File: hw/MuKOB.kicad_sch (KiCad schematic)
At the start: 46 parts, among them J10 Conn_01x04, J11 Conn_01x07, J3 Micro_SD_Card, J6 Conn_01x03, J7 SER_COM, J8 SJ-43516-SMT-TR, J9 Conn_01x02, Q2 2N3904, SW1 RESET, U1 TLV70033_SOT23-5, U2 PicoW, U3 NC7WZ16P6X, U5 MAX3221

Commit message: Schematic updates.
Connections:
- net GND: no longer C15.1, J8.T, R8.2
- net I2C0_SCL: now also J10.3 (Pin_3); no longer J10.4 (Pin_4)
- net I2C0_SDA: now also J10.4 (Pin_4); no longer J10.3 (Pin_3)
- net PWM_LL: now also C15.2, C8.1, R2.1, R4.2; no longer C14.2, C7.1, R1.1, R3.2
- net PWM_RR: now also C14.2, C7.1, R1.1, R3.2; no longer C15.2, C8.1, R2.1, R4.2
- net at J8.R1N: no longer LS1.1
- net at J8.TN: now also LS1.1
- new net PWM_AUDIO_L: C15.1, J8.T, R8.2
- no-connect marks 5 -> 6
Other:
- note added: "3.5mm TRRS Audio (STD)"
- note added: "Audio Output Option"
- note added: "Audio Section"
- note added: "Mic input (optional)"
- note added: "Needed for Analog out and/or Mic in"
- note added: "Place JR1+BZ1 or JR2+rest"
- note removed: "Audio Power"
- note removed: "Place JR1+BZ1 or JR2+LS1"
- note removed: "STD TRRS 3.5mm Audio"
- moved on the sheet: BZ1, C1, C10, C11, C12, C13, C14, C15, C16, C17, C2, C7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

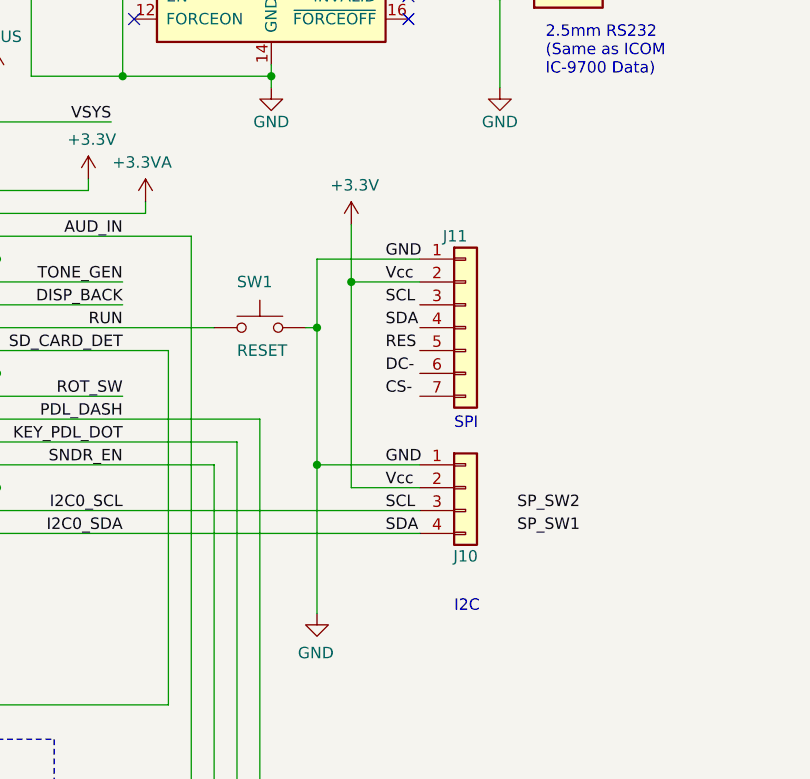
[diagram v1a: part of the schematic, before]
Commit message: Update and organize display component docs.
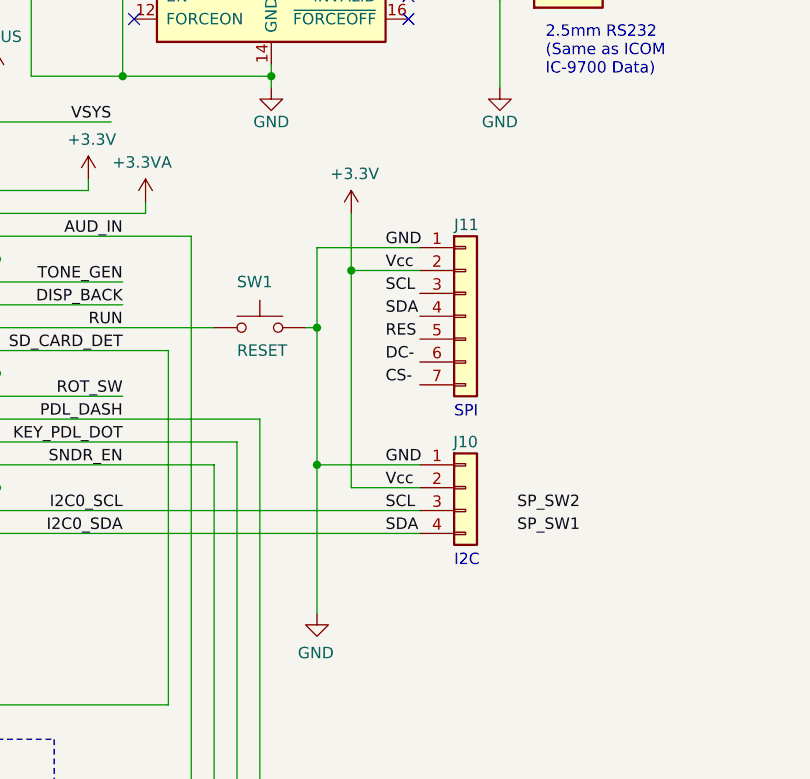
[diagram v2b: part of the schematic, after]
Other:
- moved on the sheet: J11
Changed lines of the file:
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@@
   (junction (at 31.75 173.99) (diameter 0) (color 0 0 0 0)
   )
-  (junction (at 191.77 87.63) (diameter 0) (color 0 0 0 0)
+  (junction (at 191.77 86.36) (diameter 0) (color 0 0 0 0)
   )
   (junction (at 208.28 45.72) (diameter 0) (color 0 0 0 0)
@@
     (stroke (width 0) (type default))
   )
-  (wire (pts (xy 187.96 92.71) (xy 187.96 85.09))
+  (wire (pts (xy 187.96 92.71) (xy 187.96 83.82))
     (stroke (width 0) (type default))
   )
@@
     (stroke (width 0) (type default))
   )
-  (wire (pts (xy 191.77 87.63) (xy 191.77 81.28))
+  (wire (pts (xy 191.77 86.36) (xy 191.77 80.01))
     (stroke (width 0) (type default))
   )
@@
     (stroke (width 0) (type default))
   )
-  (wire (pts (xy 191.77 87.63) (xy 199.39 87.63))
+  (wire (pts (xy 191.77 86.36) (xy 199.39 86.36))
     (stroke (width 0) (type default))
   )
@@
     (stroke (width 0) (type default))
   )
-  (wire (pts (xy 187.96 85.09) (xy 199.39 85.09))
+  (wire (pts (xy 187.96 83.82) (xy 199.39 83.82))
     (stroke (width 0) (type default))
   )
@@
     (stroke (width 0) (type default))
   )
-  (wire (pts (xy 191.77 87.63) (xy 191.77 110.49))
+  (wire (pts (xy 191.77 86.36) (xy 191.77 110.49))
     (stroke (width 0) (type default))
   )
@@
     (effects (font (size 1.27 1.27)) (justify left bottom))
   )
-  (text "I2C" (at 203.2 124.46 0)
+  (text "I2C" (at 203.2 119.38 0)
     (effects (font (size 1.27 1.27)) (justify left bottom))
   )
@@
     (effects (font (size 1.27 1.27) (color 194 0 194 1)) (justify left bottom))
   )
-  (text "SPI" (at 203.2 104.14 0)
+  (text "SPI" (at 203.2 102.87 0)
     (effects (font (size 1.27 1.27)) (justify left bottom))
   )
@@
     (effects (font (size 1.27 1.27)) (justify left bottom))
   )
-  (label "SCL" (at 195.58 90.17 0) (fields_autoplaced)
+  (label "SCL" (at 195.58 88.9 0) (fields_autoplaced)
     (effects (font (size 1.27 1.27)) (justify left bottom))
   )
@@
     (effects (font (size 1.27 1.27)) (justify right bottom))
   )
-  (label "CS-" (at 195.58 100.33 0) (fields_autoplaced)
+  (label "CS-" (at 195.58 99.06 0) (fields_autoplaced)
     (effects (font (size 1.27 1.27)) (justify left bottom))
   )
@@
     (effects (font (size 1.27 1.27)) (justify left bottom))
   )
-  (label "RES" (at 195.58 95.25 0) (fields_autoplaced)
+  (label "RES" (at 195.58 93.98 0) (fields_autoplaced)
     (effects (font (size 1.27 1.27)) (justify left bottom))
   )
@@
     (effects (font (size 1.27 1.27)) (justify right bottom))
   )
-  (label "SDA" (at 195.58 92.71 0) (fields_autoplaced)
+  (label "SDA" (at 195.58 91.44 0) (fields_autoplaced)
     (effects (font (size 1.27 1.27)) (justify left bottom))
   )
@@
     (effects (font (size 1.27 1.27)) (justify left bottom))
   )
-  (label "DC-" (at 195.58 97.79 0) (fields_autoplaced)
+  (label "DC-" (at 195.58 96.52 0) (fields_autoplaced)
     (effects (font (size 1.27 1.27)) (justify left bottom))
   )
@@
     (effects (font (size 1.27 1.27)) (justify left bottom))
   )
-  (label "Vcc" (at 195.58 87.63 0) (fields_autoplaced)
+  (label "Vcc" (at 195.58 86.36 0) (fields_autoplaced)
     (effects (font (size 1.27 1.27)) (justify left bottom))
   )
@@
     (effects (font (size 1.27 1.27)) (justify left bottom))
   )
-  (label "GND" (at 195.58 85.09 0) (fields_autoplaced)
+  (label "GND" (at 195.58 83.82 0) (fields_autoplaced)
     (effects (font (size 1.27 1.27)) (justify left bottom))
   )
@@
     )
   )
-  (symbol (lib_id "Connector_Generic:Conn_01x07") (at 204.47 92.71 0) (unit 1)
-    (in_bom yes) (on_board yes) (dnp no)
-    (property "Reference" "J11" (at 201.93 82.55 0)
-      (effects (font (size 1.27 1.27)) (justify left))
-    )
-    (property "Value" "Conn_01x07" (at 207.01 94.615 0)
+  (symbol (lib_id "Connector_Generic:Conn_01x07") (at 204.47 91.44 0) (unit 1)
+    (in_bom yes) (on_board yes) (dnp no)
+    (property "Reference" "J11" (at 203.2 81.28 0)
+      (effects (font (size 1.27 1.27)) (justify left))
+    )
+    (property "Value" "Conn_01x07" (at 207.01 93.345 0)
       (effects (font (size 1.27 1.27)) (justify left) hide)
     )
-    (property "Footprint" "" (at 204.47 92.71 0)
-      (effects (font (size 1.27 1.27)) hide)
-    )
-    (property "Datasheet" "~" (at 204.47 92.71 0)
+    (property "Footprint" "" (at 204.47 91.44 0)
+      (effects (font (size 1.27 1.27)) hide)
+    )
+    (property "Datasheet" "~" (at 204.47 91.44 0)
       (effects (font (size 1.27 1.27)) hide)
     )
@@
   (symbol (lib_id "Connector_Generic:Conn_01x04") (at 204.47 110.49 0) (unit 1)
     (in_bom yes) (on_board yes) (dnp no)
-    (property "Reference" "J10" (at 204.47 118.11 0)
+    (property "Reference" "J10" (at 204.47 105.41 0)
       (effects (font (size 1.27 1.27)))
     )
@@
     )
   )
-  (symbol (lib_id "power:+3.3V") (at 191.77 81.28 0) (unit 1)
-    (in_bom yes) (on_board yes) (dnp no)
-    (property "Reference" "#PWR024" (at 191.77 85.09 0)
-      (effects (font (size 1.27 1.27)) hide)
-    )
-    (property "Value" "+3.3V" (at 192.151 76.8858 0)
-      (effects (font (size 1.27 1.27)))
-    )
-    (property "Footprint" "" (at 191.77 81.28 0)
-      (effects (font (size 1.27 1.27)) hide)
-    )
-    (property "Datasheet" "" (at 191.77 81.28 0)
-      (effects (font (size 1.27 1.27)) hide)
-    )
+  (symbol (lib_id "power:+3.3V") (at 191.77 80.01 0) (unit 1)
+    (in_bom yes) (on_board yes) (dnp no)
+    (property "Reference" "#PWR024" (at 191.77 83.82 0)
+      (effects (font (size 1.27 1.27)) hide)
+    )
+    (property "Value" "+3.3V" (at 192.151 75.6158 0)
+      (effects (font (size 1.27 1.27)))
+    )
+    (property "Footprint" "" (at 191.77 80.01 0)
+      (effects (font (size 1.27 1.27)) hide)
+    )
+    (property "Datasheet" "" (at 191.77 80.01 0)
+      (effects (font (size 1.27 1.27)) hide)
+    )

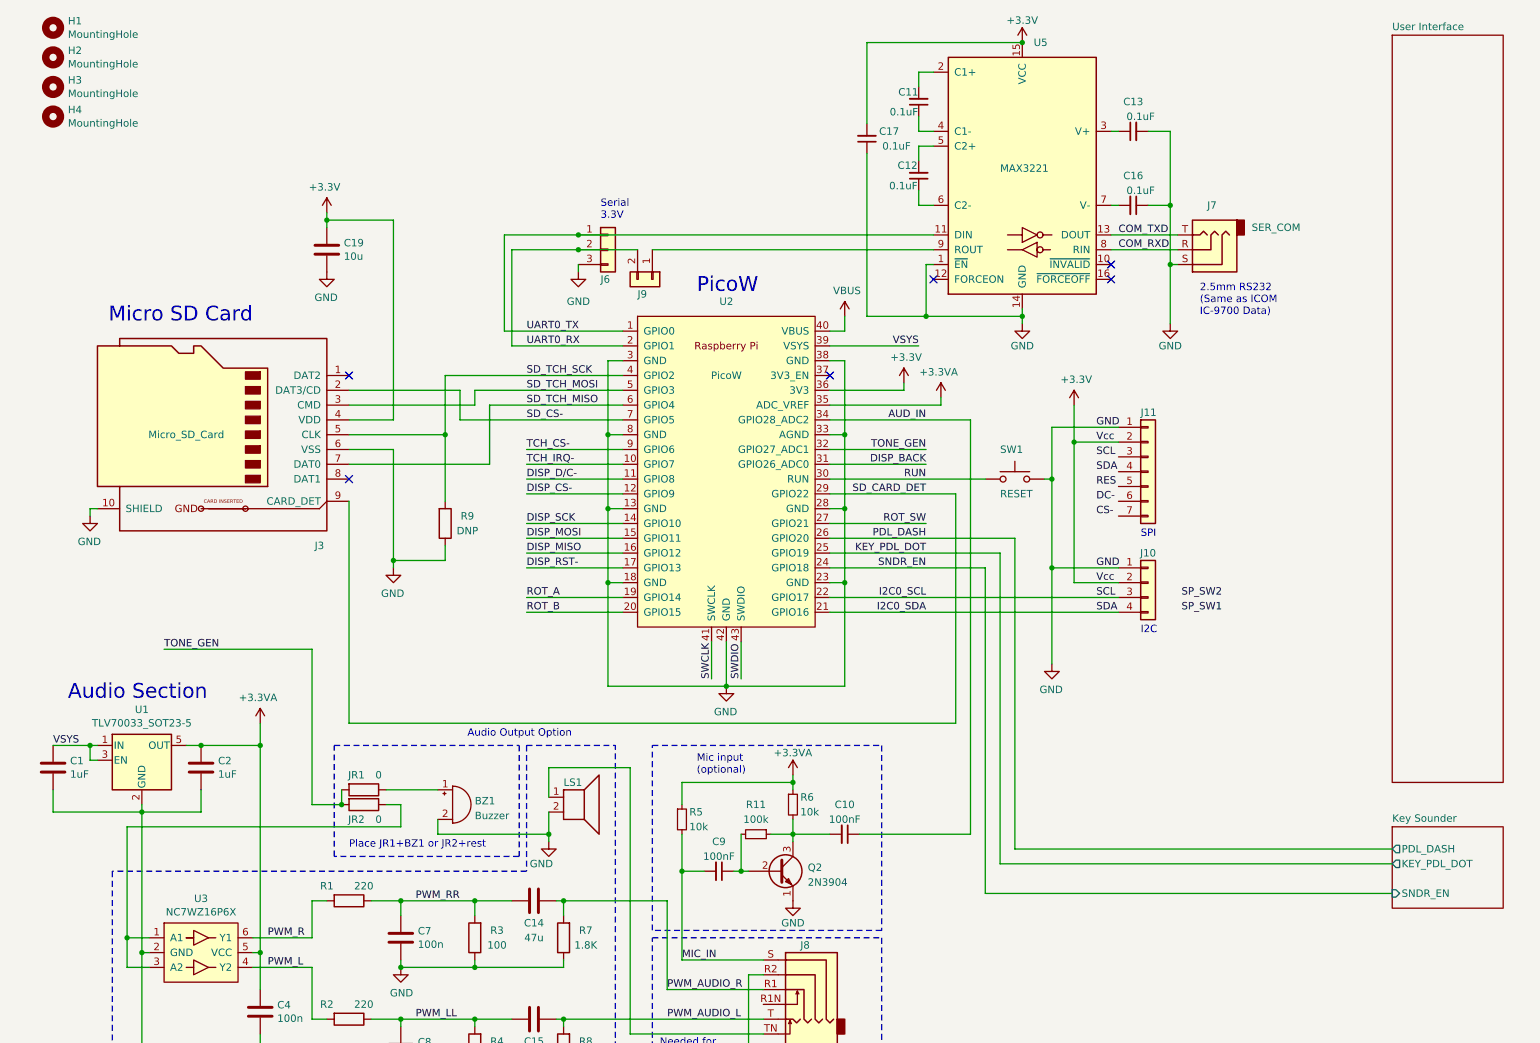
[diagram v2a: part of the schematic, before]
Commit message: HW - Display FFCs.
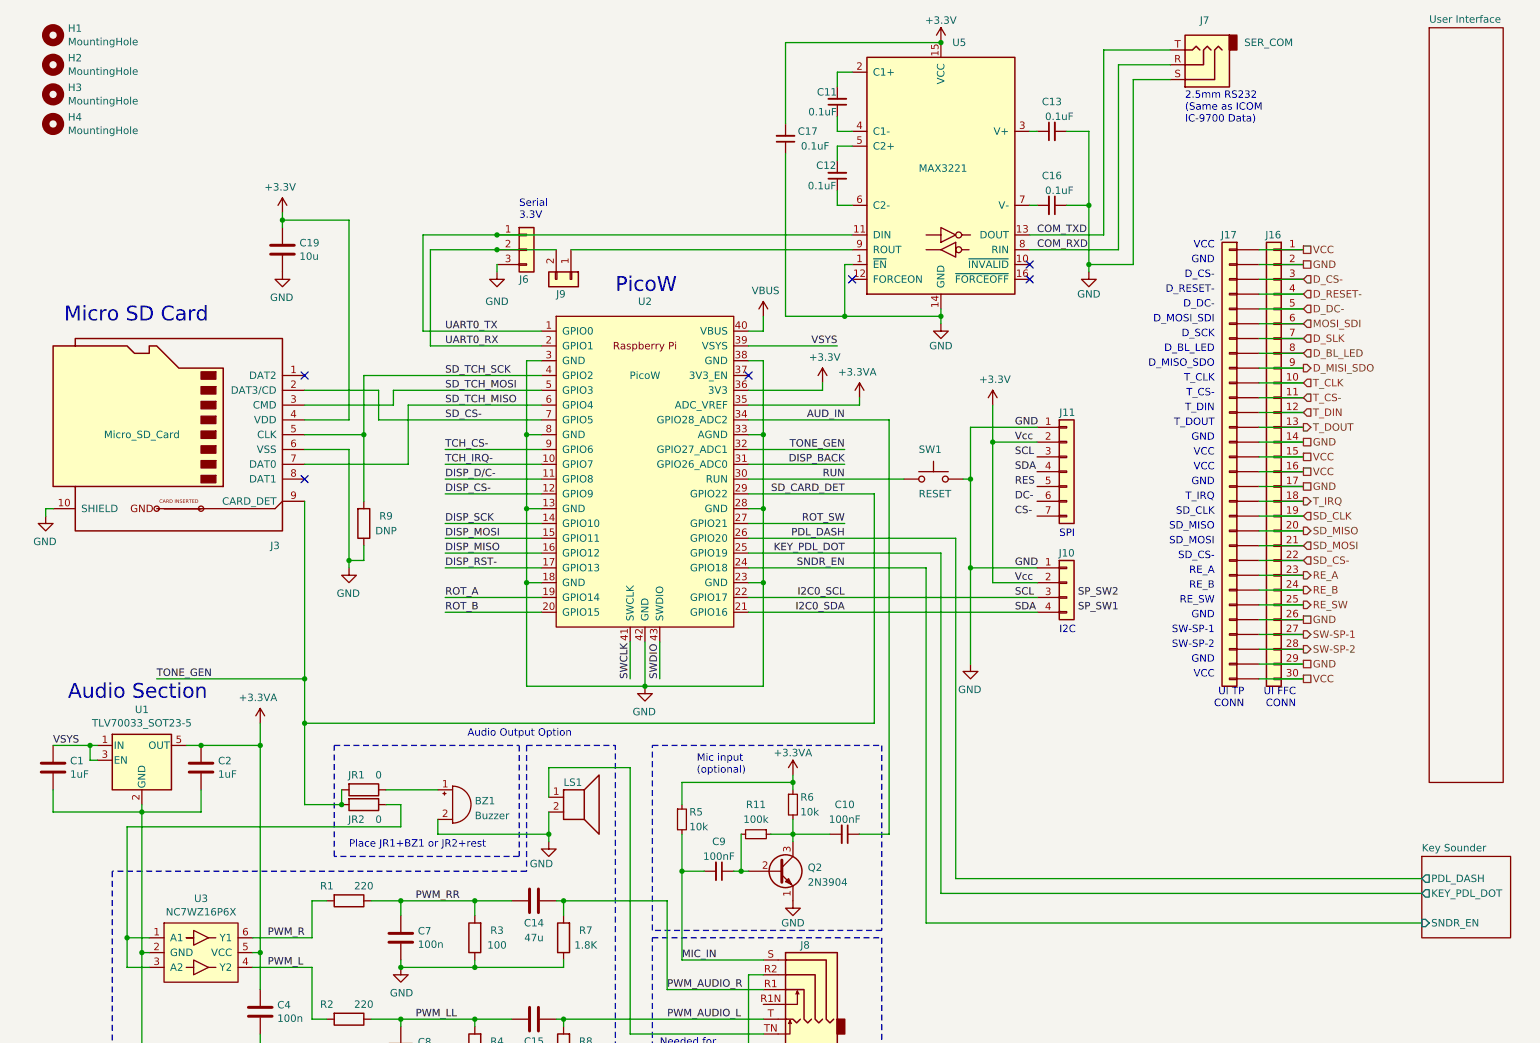
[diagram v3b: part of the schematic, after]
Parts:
- added J16, J17: Conn_01x30, symbol Connector_Generic:Conn_01x30
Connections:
- net TONE_GEN is gone; now on net SD_CARD_DET: JR1.2, JR2.2, U2.32 (GPIO27_ADC1)
- net GND: now also J16.14 (Pin_14), J16.17 (Pin_17), J16.2 (Pin_2), J16.26 (Pin_26), J16.29 (Pin_29), J17.14 (Pin_14), J17.17 (Pin_17), J17.2 (Pin_2), J17.26 (Pin_26), J17.29 (Pin_29)
- net SD_CS-: now also J16.22 (Pin_22), J17.22 (Pin_22)
- new net D_BL_LED: J16.8 (Pin_8), J17.8 (Pin_8)
- new net D_CS-: J16.3 (Pin_3), J17.3 (Pin_3)
- new net D_DC-: J16.5 (Pin_5), J17.5 (Pin_5)
- new net D_MISI_SDO: J16.9 (Pin_9), J17.9 (Pin_9)
- new net D_RESET-: J16.4 (Pin_4), J17.4 (Pin_4)
- new net D_SLK: J16.7 (Pin_7), J17.7 (Pin_7)
- new net MOSI_SDI: J16.6 (Pin_6), J17.6 (Pin_6)
- new net RE_A: J16.23 (Pin_23), J17.23 (Pin_23)
- new net RE_B: J16.24 (Pin_24), J17.24 (Pin_24)
- new net RE_SW: J16.25 (Pin_25), J17.25 (Pin_25)
- new net SD_CLK: J16.19 (Pin_19), J17.19 (Pin_19)
- new net SD_MISO: J16.20 (Pin_20), J17.20 (Pin_20)
- new net SD_MOSI: J16.21 (Pin_21), J17.21 (Pin_21)
- new net SW-SP-1: J16.27 (Pin_27), J17.27 (Pin_27)
- new net SW-SP-2: J16.28 (Pin_28), J17.28 (Pin_28)
- new net T_CLK: J16.10 (Pin_10), J17.10 (Pin_10)
- new net T_CS-: J16.11 (Pin_11), J17.11 (Pin_11)
- new net T_DIN: J16.12 (Pin_12), J17.12 (Pin_12)
- new net T_DOUT: J16.13 (Pin_13), J17.13 (Pin_13)
- new net T_IRQ: J16.18 (Pin_18), J17.18 (Pin_18)
- new net VCC: J16.1 (Pin_1), J16.15 (Pin_15), J16.16 (Pin_16), J16.30 (Pin_30), J17.1 (Pin_1), J17.15 (Pin_15), J17.16 (Pin_16), J17.30 (Pin_30)
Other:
- note added: "D_BL_LED"
- note added: "D_CS-"
- note added: "D_DC-"
- note added: "D_MISO_SDO"
- note added: "D_MOSI_SDI"
- note added: "D_RESET-"
- note added: "D_SCK"
- note added: "GND"
- note added: "RE_A"
- note added: "RE_B"
- note added: "RE_SW"
- note added: "SD_CLK"
- note added: "SD_CS-"
- note added: "SD_MISO"
- note added: "SD_MOSI"
- note added: "SW-SP-1"
- note added: "SW-SP-2"
- note added: "T_CLK"
- note added: "T_CS-"
- note added: "T_DIN"
- note added: "T_DOUT"
- note added: "T_IRQ"
- note added: "UI FFC CONN"
- note added: "UI TP CONN"
- note added: "VCC"
- moved on the sheet: C11, C12, C13, C16, C17, C19, H1, H2, H3, H4, J10, J11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

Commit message: Finish KOB page. UI FFC on.
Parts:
- removed J17: Conn_01x30, symbol Connector_Generic:Conn_01x30
- added J14: SPKR, symbol Connector_Generic:Conn_01x02
- added J17: Conn_02x15_Odd_Even, symbol Connector_Generic:Conn_02x15_Odd_Even
- renumbered H1 to M_H1, H2 to M_H2, H3 to M_H3, H4 to M_H4
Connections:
- net D_BL_LED is gone; now on net DISP_BL_LED: J16.8 (Pin_8)
- net D_CS- is gone; now on net DISP_CS-: J16.3 (Pin_3)
- net D_DC- is gone; now on net DISP_D/C-: J16.5 (Pin_5)
- net D_MISI_SDO is gone; now on net DISP_MISO: J16.9 (Pin_9)
- net D_RESET- is gone; now on net DISP_RST-: J16.4 (Pin_4)
- net D_SLK is gone; now on net DISP_SCK: J16.7 (Pin_7)
- net MOSI_SDI is gone; now on net DISP_MOSI: J16.6 (Pin_6)
- net ROT_A is gone; now on net RE_A: U2.19 (GPIO14)
- net ROT_B is gone; now on net RE_B: U2.20 (GPIO15)
- net SD_TCH_SCK is gone; now on net SD_CARD_DET: J3.5 (CLK), R9.2, U2.4 (GPIO2)
- net VCC is gone; now on net +3V3: J16.1 (Pin_1), J16.15 (Pin_15), J16.16 (Pin_16), J16.30 (Pin_30)
- net +3V3: now also J17.1 (Pin_1), J17.15 (Pin_15), J17.16 (Pin_16), J17.30 (Pin_30)
- net DISP_CS-: now also J17.3 (Pin_3)
- net DISP_D/C-: now also J17.5 (Pin_5)
- net DISP_MISO: now also J17.9 (Pin_9)
- net DISP_MOSI: now also J17.6 (Pin_6)
- net DISP_RST-: now also J17.4 (Pin_4)
- net DISP_SCK: now also J17.7 (Pin_7)
- net GND: now also J14.2 (Pin_2), J17.14 (Pin_14), J17.17 (Pin_17), J17.2 (Pin_2), J17.26 (Pin_26), J17.29 (Pin_29); no longer LS1.2
- net RE_A: no longer J16.23 (Pin_23)
- net RE_B: no longer J16.24 (Pin_24)
- net SD_CARD_DET: no longer JR1.2, JR2.2, U2.32 (GPIO27_ADC1)
- net SD_CS-: no longer J16.22 (Pin_22)
- net at J8.TN: now also J14.1 (Pin_1); no longer LS1.1
- net DISP_BACK renamed DISP_BL_LED
- net DISP_BL_LED: now also J17.8 (Pin_8)
- net RE_SW renamed User Interface/RE_SW
- net User Interface/RE_SW: now also J17.25 (Pin_25)
- net SD_CLK renamed User Interface/SD_CLK
- net User Interface/SD_CLK: now also J17.19 (Pin_19)
- net SD_MISO renamed User Interface/SD_MISO
- net User Interface/SD_MISO: now also J17.20 (Pin_20)
- net SD_MOSI renamed User Interface/SD_MOSI
- net User Interface/SD_MOSI: now also J17.21 (Pin_21)
- net SW-SP-1 renamed User Interface/SW-SP-1
- net User Interface/SW-SP-1: now also J17.27 (Pin_27)
- net SW-SP-2 renamed User Interface/SW-SP-2
- net User Interface/SW-SP-2: now also J17.28 (Pin_28)
- net T_CLK renamed User Interface/T_CLK
- net User Interface/T_CLK: now also J17.10 (Pin_10)
- net T_CS- renamed User Interface/T_CS-
- net User Interface/T_CS-: now also J17.11 (Pin_11)
- net T_DIN renamed User Interface/T_DIN
- net User Interface/T_DIN: now also J17.12 (Pin_12)
- net T_DOUT renamed User Interface/T_DOUT
- net User Interface/T_DOUT: now also J17.13 (Pin_13)
- net T_IRQ renamed User Interface/T_IRQ
- net User Interface/T_IRQ: now also J17.18 (Pin_18)
- new net TONE_GEN: JR1.2, JR2.2, U2.32 (GPIO27_ADC1)
- new net User Interface/RE_A: J16.23 (Pin_23), J17.23 (Pin_23)
- new net User Interface/RE_B: J16.24 (Pin_24), J17.24 (Pin_24)
- new net User Interface/SD_CS-: J16.22 (Pin_22), J17.22 (Pin_22)
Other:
- sheet User Interface ports: added D_BL_LED, D_CS-, D_DC-, D_MISO_SDO, D_MOSI_SDI, D_RESET-, D_SLK, GND, RE_A, RE_B, RE_SW, SD_CLK, SD_CS-, SD_MISO, SD_MOSI, SW-SP-1, SW-SP-2, T_CLK, T_CS-, T_DIN, T_DOUT, T_IRQ, VCC; removed none
- note added: "I2C-0"
- note added: "SPI-0"
- note added: "Serial Data Comm"
- note added: "UI RC"
- note added: "User Interface FFC Connector"
- note removed: "D_BL_LED"
- note removed: "D_CS-"
- note removed: "D_DC-"
- note removed: "D_MISO_SDO"
- note removed: "D_MOSI_SDI"
- note removed: "D_RESET-"
- note removed: "D_SCK"
- note removed: "I2C"
- note removed: "SPI"
- note removed: "T_CLK"
- note removed: "T_CS-"
- note removed: "T_DIN"
- note removed: "T_DOUT"
- note removed: "UI FFC CONN"
- note removed: "UI TP CONN"
- moved on the sheet: BZ1, C1, C10, C11, C12, C13, C14, C15, C16, C17, C19, C2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
